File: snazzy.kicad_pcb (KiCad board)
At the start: 2 copper layers, 57.8 x 53.3 mm, 34 parts, among them J1 Conn_01x03, J2 Conn_01x03, SW1 BTN_START, SW10 BTN_DOWN, SW11 BTN_L, SW12 BTN_R, SW2 BTN_SELECT, SW3 BTN_A, SW4 BTN_B, SW5 BTN_X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

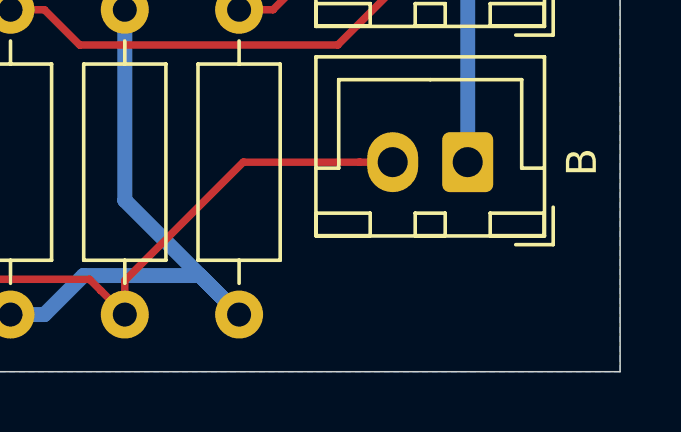
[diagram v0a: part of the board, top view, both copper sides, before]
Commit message: PCB: Add revision number silkscreen
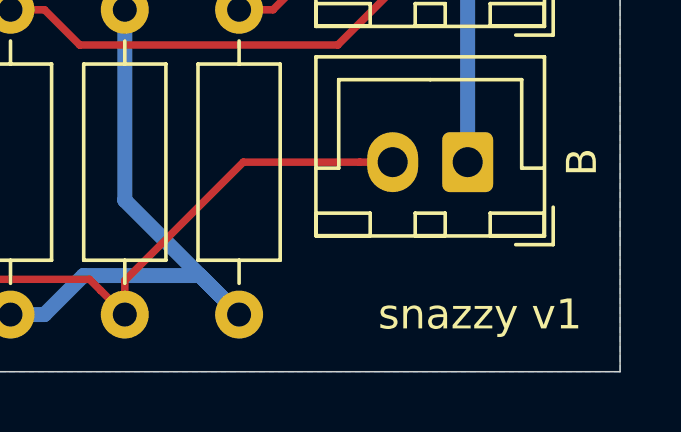
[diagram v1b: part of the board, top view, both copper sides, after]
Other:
- board text added: "snazzy v1"
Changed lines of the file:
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@@
   (general
     (thickness 1.6)
-    (drawings 6)
+    (drawings 7)
     (tracks 348)
     (zones 0)
@@
   (title_block
     (title "snazzy SNES controller")
+    (rev v1)
   )
   (layers
@@
     )
   )
+  (gr_text "snazzy v1" (at 164.465 125.73) (layer F.SilkS)
+    (effects (font (size 1 1) (thickness 0.15)) (justify right))
+  )
   (dimension 53.34 (width 0.12) (layer F.Fab)

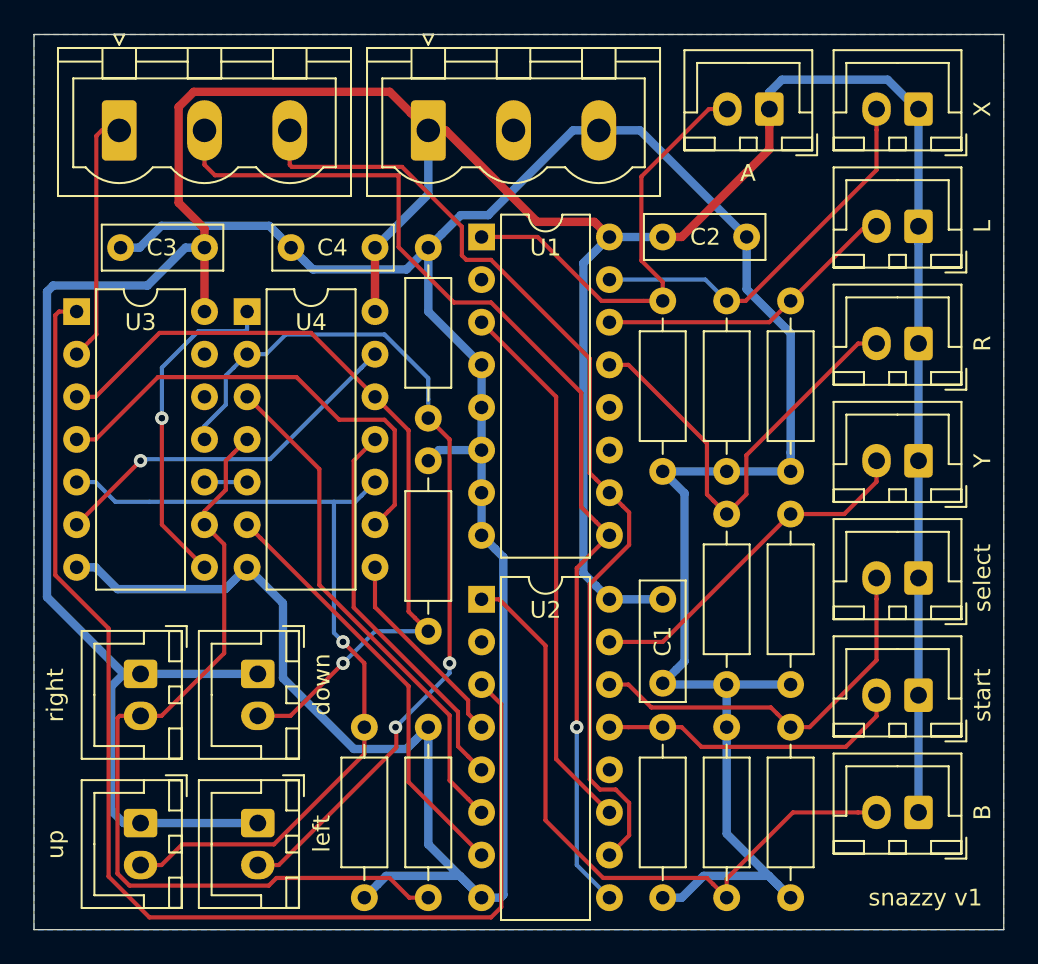
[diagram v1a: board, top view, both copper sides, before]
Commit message: PCB: Clean up traces a bit to reduce ground loops
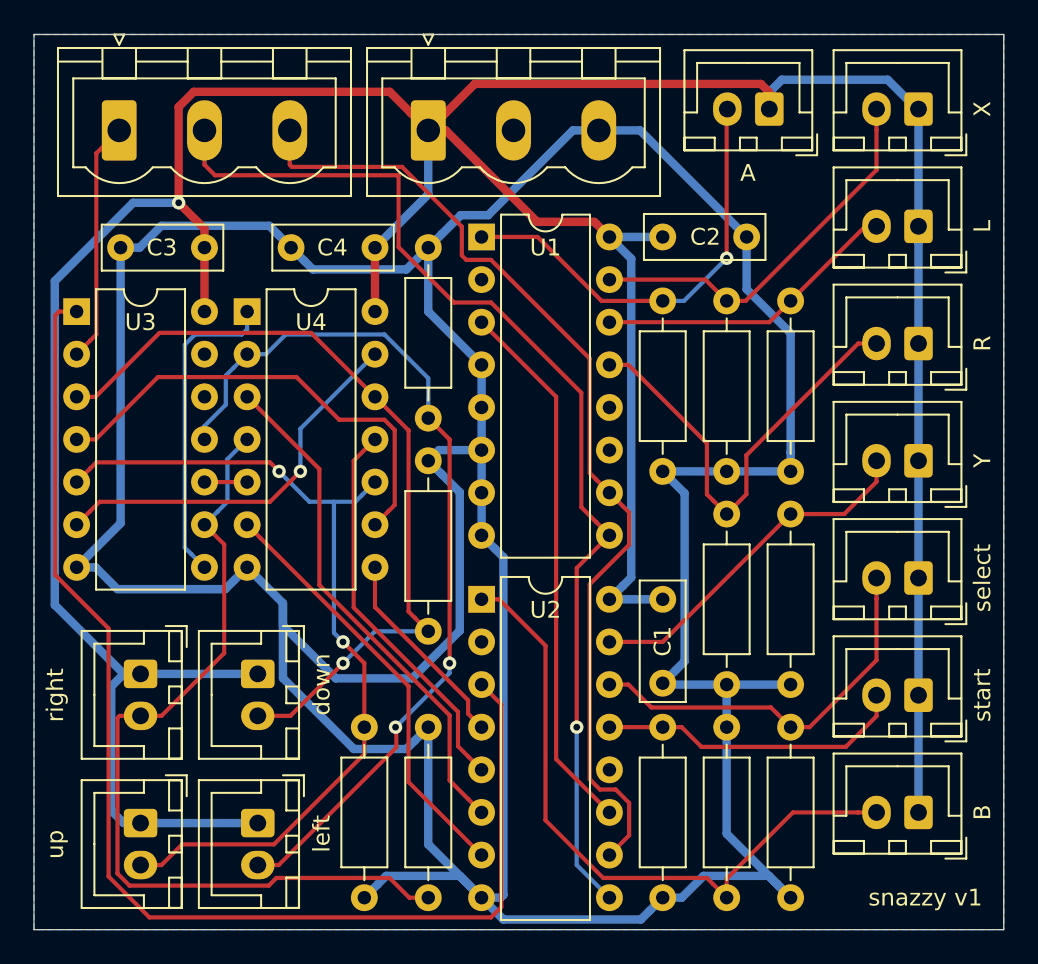
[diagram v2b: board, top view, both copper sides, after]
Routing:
- net GND: track 206.4 -> 263.7 mm
- net +5V: track 208.2 -> 219.0 mm, vias 0 -> 1
- net Net-(U3-Pad6): track 22.0 -> 23.5 mm
- net Net-(U3-Pad8): track 20.0 -> 18.9 mm, vias 1 -> 0
- net /BTN_UP: track 51.2 -> 52.2 mm, vias 1 -> 2
- net /BTN_A: track 27.1 -> 26.1 mm, vias 0 -> 1
- net SNES_data1: track 15.0 -> 14.4 mm
